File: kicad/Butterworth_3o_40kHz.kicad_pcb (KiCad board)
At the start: 2 copper layers, 40.6 x 48.5 mm, 30 parts, among them J1 Conn_01x02_Pin, J2 Conn_01x02_Pin, J3 Conn_01x03_Pin, J4 Conn_01x02_Pin, J5 Conn_01x02_Pin, J6 Conn_01x02_Pin, J7 Conn_01x02_Pin, U1 TL072, U2 LM317L_TO92, U3 LMC7660

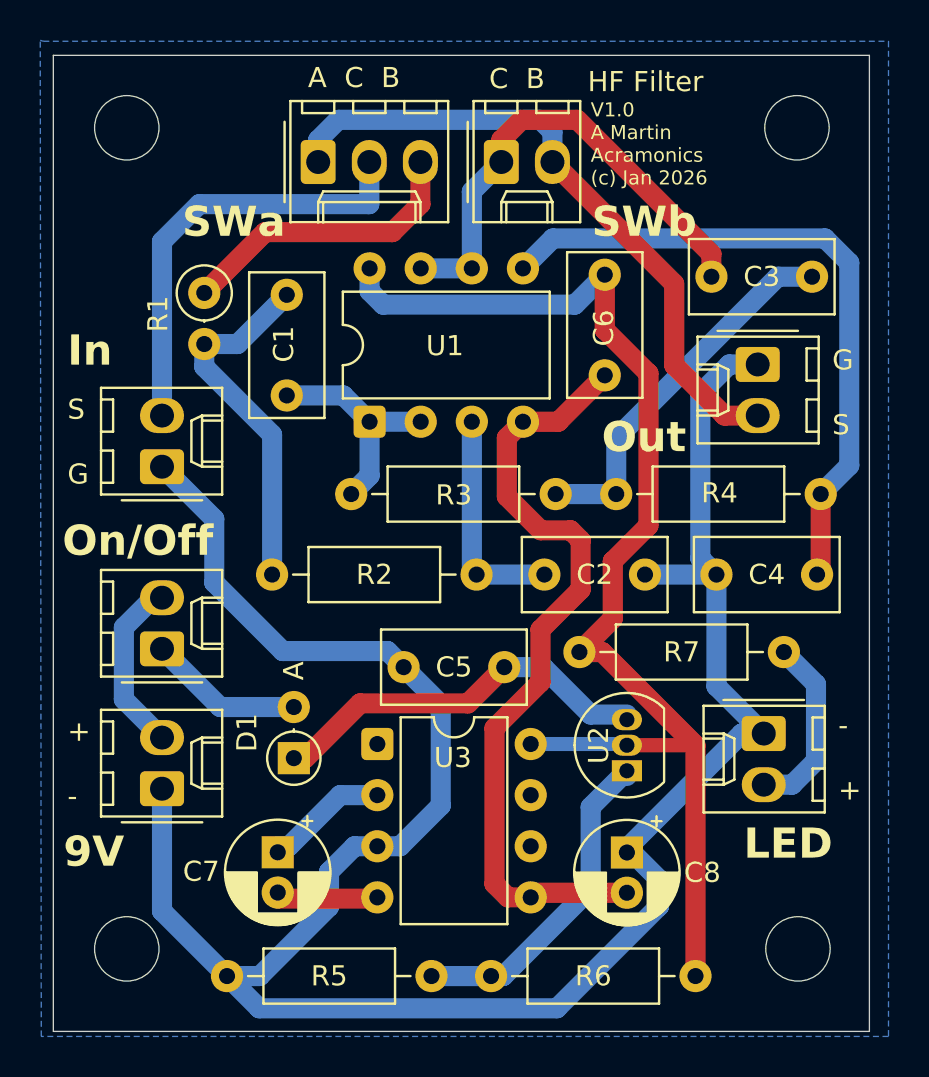
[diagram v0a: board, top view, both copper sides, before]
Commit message: Added annotation of the PSU section to the PCB
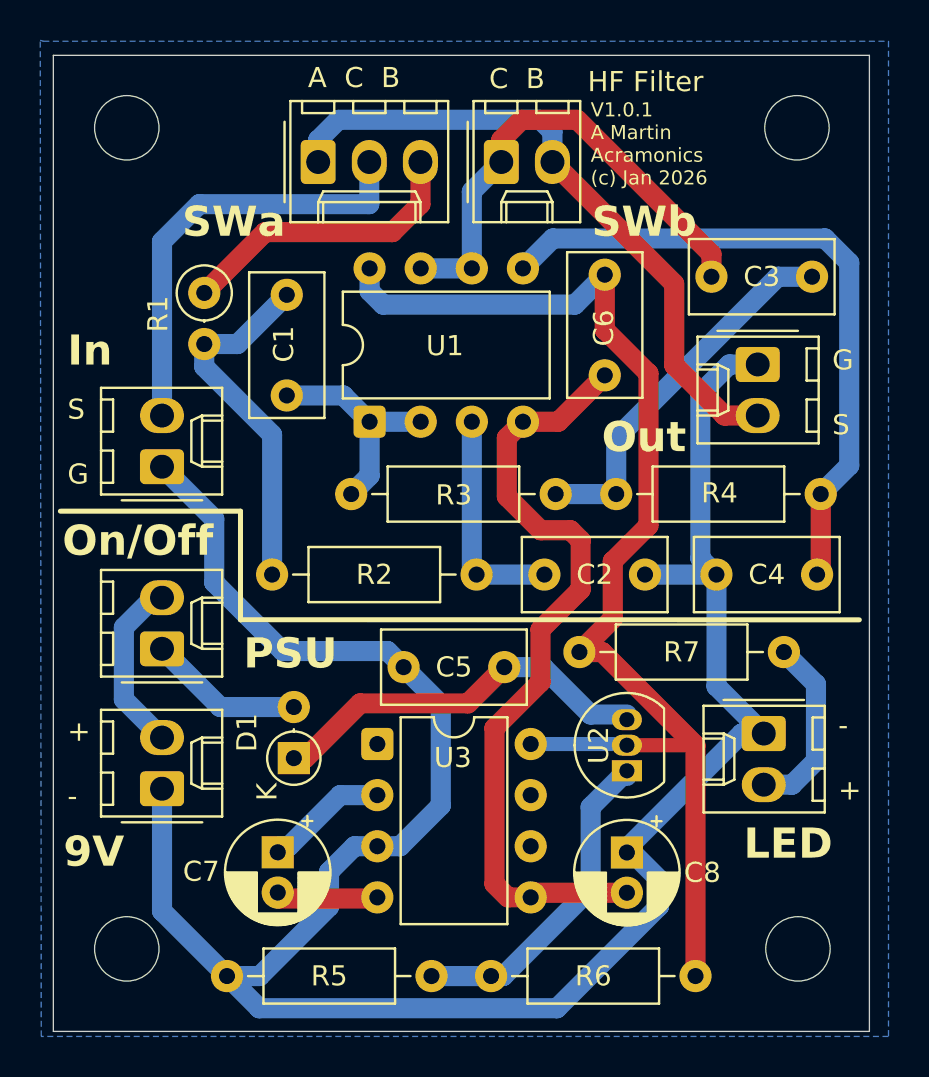
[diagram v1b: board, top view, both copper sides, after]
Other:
- board text added: "PSU"
- board text added: "V1.0.1 A Martin Acramonics (c) Jan 2026"
- board text removed: "V1.0 A Martin Acramonics (c) Jan 2026"
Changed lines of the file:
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@@
 			(layer "F.Fab")
 		)
-		(fp_text user "A"
-			(at 4.34 0 90)
+		(fp_text user "K"
+			(at -1.677817 -1.326371 90)
 			(layer "F.SilkS")
 			(effects
@@
 		(embedded_fonts no)
 	)
+	(gr_line
+		(start 43.7 117.35)
+		(end 52.65 117.35)
+		(stroke
+			(width 0.25)
+			(type solid)
+		)
+		(layer "F.SilkS")
+	)
+	(gr_line
+		(start 52.65 117.35)
+		(end 52.65 122.75)
+		(stroke
+			(width 0.25)
+			(type solid)
+		)
+		(layer "F.SilkS")
+	)
+	(gr_line
+		(start 52.65 122.743463)
+		(end 83.4 122.75)
+		(stroke
+			(width 0.25)
+			(type solid)
+		)
+		(layer "F.SilkS")
+	)
 	(gr_rect
 		(start 43.35 94.7)
@@
 		)
 	)
+	(gr_text "PSU"
+		(at 52.8 125.3 0)
+		(layer "F.SilkS")
+		(effects
+			(font
+				(size 1.5 1.5)
+				(thickness 0.3)
+				(bold yes)
+			)
+			(justify left bottom)
+		)
+	)
 	(gr_text "G\n\nS"
 		(at 82.05 113.65 0)
@@
 		)
 	)
-	(gr_text "V1.0\nA Martin\nAcramonics\n(c) Jan 2026"
+	(gr_text "V1.0.1\nA Martin\nAcramonics\n(c) Jan 2026"
 		(at 70.05 101.2 0)
 		(layer "F.SilkS")
